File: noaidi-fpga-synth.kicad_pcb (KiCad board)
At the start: 2 copper layers, 72 parts, among them J1 DIN-5_180degree, J10 Conn_01x05_Pin, J11 Conn_01x03_Pin, J12 Conn_01x03_Pin, J13 Conn_01x03_Pin, J2 DIN-5_180degree, J3 Conn_Coaxial, J4 Conn_Coaxial, J5 Conn_01x02_Pin, J6 Conn_01x02_Pin, J7 Conn_01x04_Pin, J8 Conn_01x03_Pin, J9 USB_C_Receptacle_USB2.0_16P, U1 ESP32-S3-DevKitC, U2 Tang_Nano_20K, U3 6N138, U4 6N138, U5 Adafruit_PCM510x, U6 LM66100DCK, U7 LM66100DCK

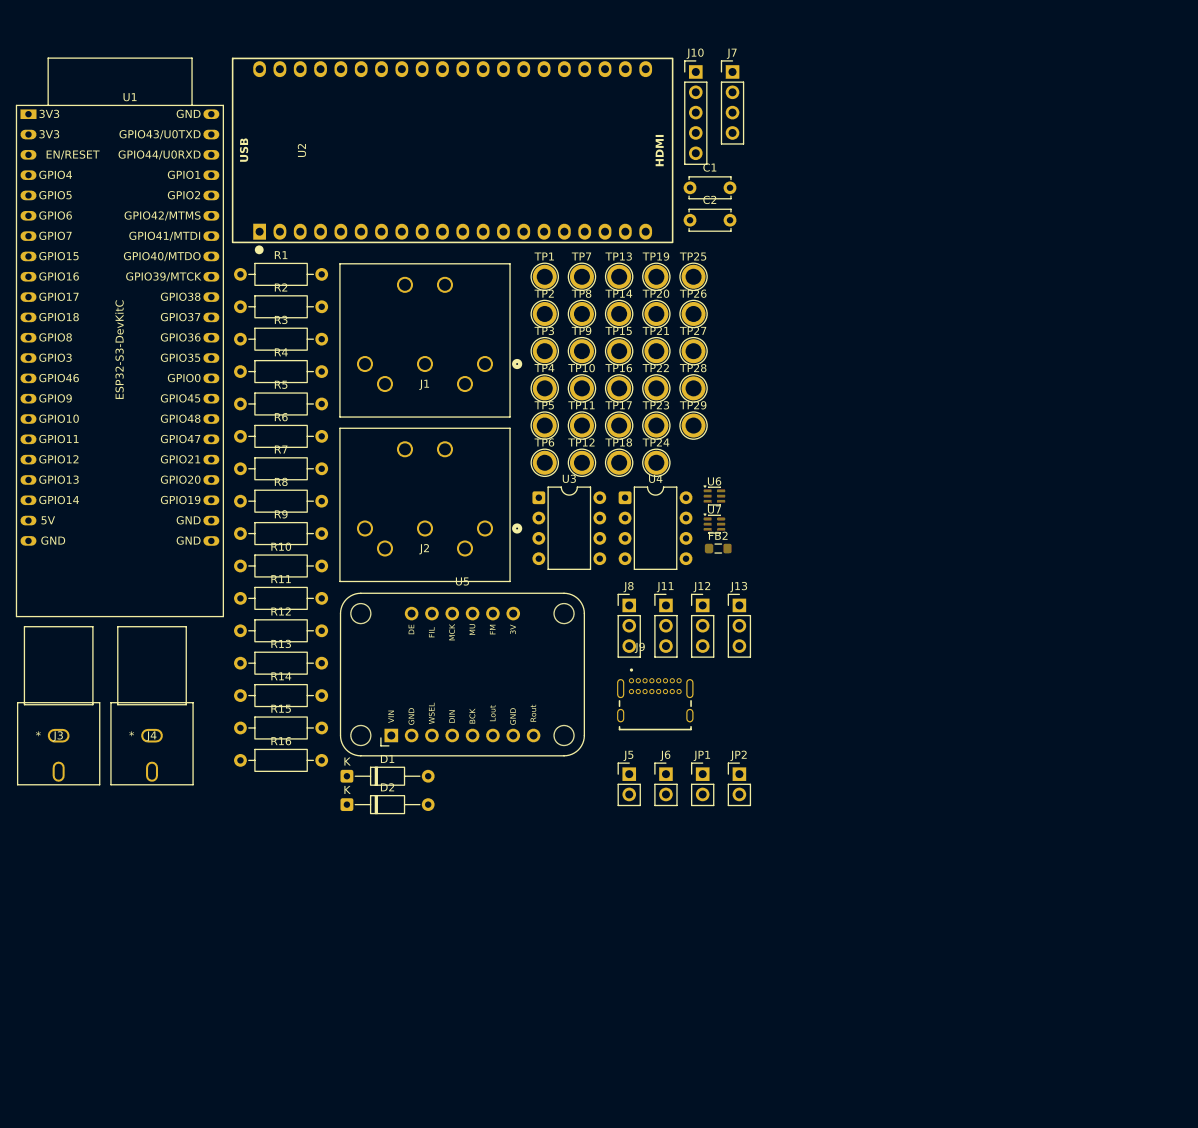
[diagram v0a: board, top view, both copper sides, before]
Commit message: Completely routed PCB
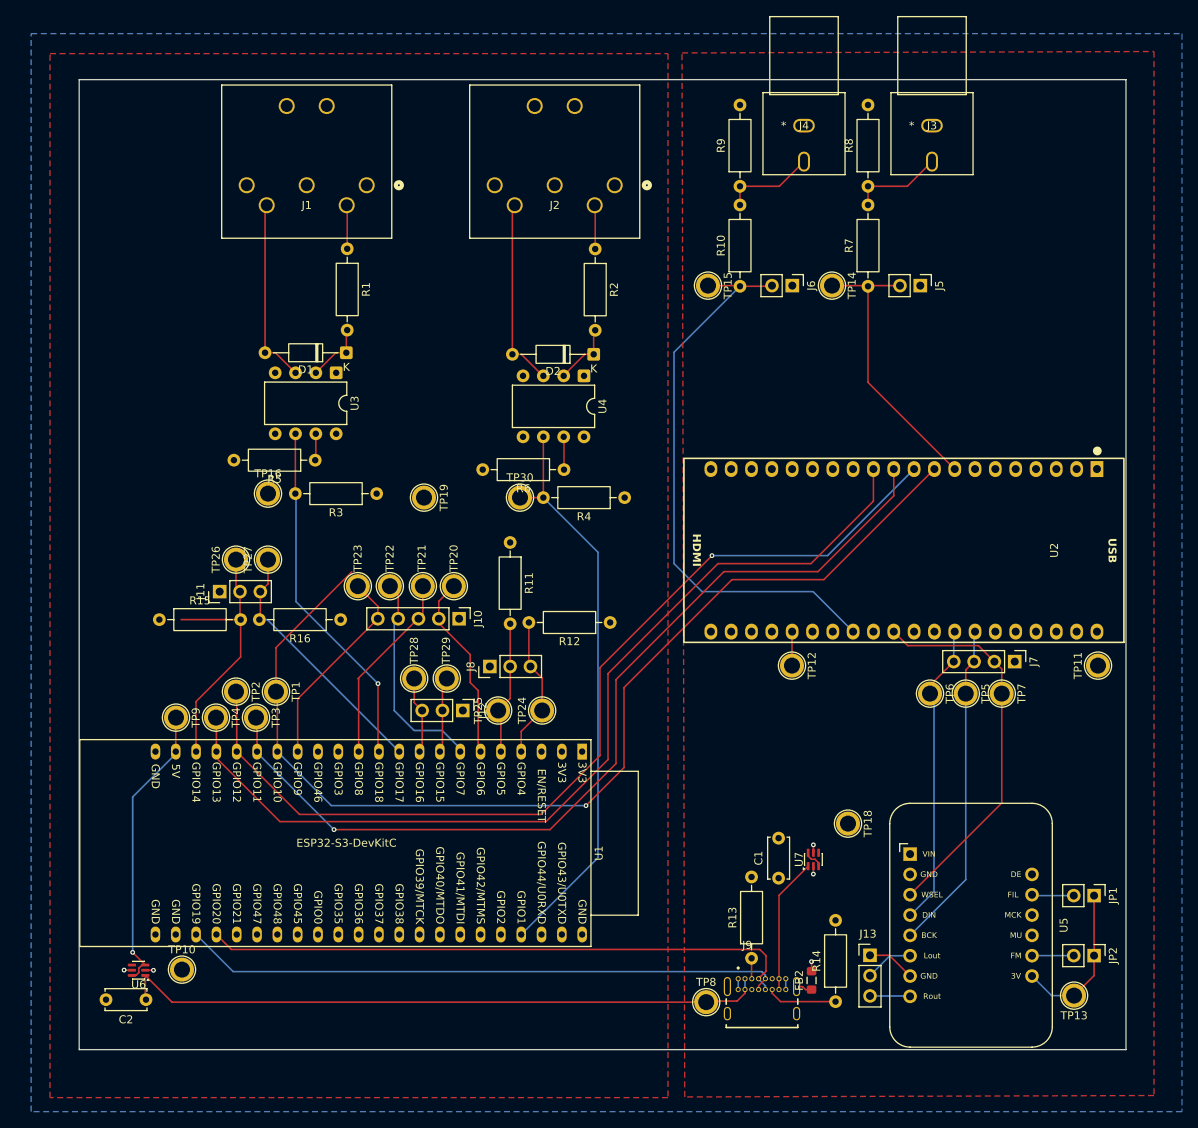
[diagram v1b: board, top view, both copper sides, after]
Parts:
- removed TP17: TestPoint, TestPoint:TestPoint_Plated_Hole_D2.0mm
- added TP30: TestPoint, TestPoint:TestPoint_Plated_Hole_D2.0mm, F.Cu at (167.0, 103.0)
- moved J3 133.2 mm to (218.5, 56.5)
- moved C2 118.8 mm to (120.2, 165.8), turned to 180 degrees
- moved J4 111.6 mm to (202.5, 56.5)
- moved TP13 106.3 mm to (236.3, 165.2), turned to 180 degrees
- moved U1 105.5 mm to (174.8, 134.8), turned to -90 degrees
- moved U6 93.2 mm to (119.3, 162.1), turned to 180 degrees
- moved TP10 88.2 mm to (124.8, 162.0)
- moved R8 87.8 mm to (210.5, 64.1), turned to 90 degrees
- moved TP8 87.4 mm to (190.3, 166.1)
- moved C1 87.0 mm to (199.3, 150.6), turned to 90 degrees
- moved R14 83.6 mm to (206.4, 166.0), turned to 90 degrees
- moved J7 81.7 mm to (228.8, 123.5), turned to -90 degrees
- moved R7 81.7 mm to (210.5, 76.6), turned to 90 degrees
- moved R9 76.1 mm to (194.5, 64.1), turned to 90 degrees
- moved U2 75.4 mm to (215.0, 109.6), turned to 180 degrees
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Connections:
- TP29 pad 1: ESP_UART0_RX -> ESP_UART0_TX
- U2 pad 19: NANO_3V3 -> unconnected-(U2-3V3-Pad19)
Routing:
- net SPI2_CS_N: track 0.00 -> 134.7 mm, vias 0 -> 1
- net SPI2_SCLK: track 0.00 -> 119.8 mm, vias 0 -> 1
- net SPI2_MISO: track 0.00 -> 117.4 mm
- net SPI2_MOSI: track 0.00 -> 114.8 mm, vias 0 -> 1
- net EXT_5V: track 0.00 -> 100.0 mm
- net USB_D-: track 0.00 -> 75.4 mm
- net USB_D+: track 0.00 -> 74.8 mm
- net SPDIF1: track 0.00 -> 72.1 mm
- net ESP_UART2_RX: track 0.00 -> 71.9 mm
- net I2S_WS: track 0.00 -> 48.4 mm
- net ESP_UART1_RX: track 0.00 -> 44.1 mm, vias 0 -> 1
- net I2S_BCK: track 0.00 -> 41.3 mm
- net I2S_DATA: track 0.00 -> 38.2 mm
- net ESP_5V: track 0.00 -> 36.9 mm, vias 0 -> 1
- net SPDIF0: track 0.00 -> 35.9 mm
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- added copper zone on F.Cu, net ESP_3V3
- added copper zone on B.Cu, net GND
- added copper zone on F.Cu, net NANO_5V
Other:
- board outline added: 130.8 x 121.2 mm

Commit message: PCB fixes
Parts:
- moved J3 5.75 mm to (224.2, 56.5)
- moved J5 5.75 mm to (222.8, 76.5)
- moved R7 5.75 mm to (216.2, 76.6)
- moved R8 5.75 mm to (216.2, 64.1)
- moved TP14 5.75 mm to (211.8, 76.5)
- moved R12 0.33 mm to (178.6, 118.5)
- turned TP5 to 0 degrees
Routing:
- net GND: track 7.89 -> 27.0 mm
- net SPI2_CS_N: track 134.7 -> 115.8 mm
- net I2C1_SCL: track 34.0 -> 26.6 mm
- net EXT_5V: track 100.0 -> 107.2 mm
- net SPDIF0: track 35.9 -> 31.9 mm
- net ESP_UART1_RX: track 44.1 -> 47.5 mm
- net USB_D+: track 74.8 -> 73.9 mm
